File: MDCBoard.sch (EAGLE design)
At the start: 201 parts, among them J1 JUMPER-SOLDER, J10 USB-C-RECEPTACLE-KOREANHRO, J2 JUMPER-SOLDER, J3 JUMPER-SOLDER, J4 JUMPER-SOLDER, J5 JST-SM02B-SRSS-TB, J6 JUMPER-SOLDER, J7 JUMPER-SOLDER, J8 JUMPER-SOLDER, J9 MICROSD-SOCKET, Q1 PMOS-NEXPERIA-SOT1220, Q2 PMOS-NEXPERIA-SOT1220, Q3 PMOS-NEXPERIA-SOT1220, Q4 DIODESINC-DMG2305UX, Q5 DIODESINC-DMG2305UX, Q6 DIODESINC-DMG2305UX, Q7 DIODESINC-DMG2305UX, Q8 DIODESINC-DMG2305UX, SW1 TACTILE-SWITCH, U1 TI-TPS2116, U10 TI-TPS22919DCK, U11 TI-TPS22919DCK, U12 TI-TPS22919DCK, U13 TI-TPS22919DCK, U14 TI-MSP430FR2433IRGE, U15 TI-TXB0102, U16 PANASONIC-EKMB110711X, U17 LATTICE-ICE40HX4K-BG121, U18 WINBOND-W25Q40EW, U19 NEXPERIA-74LVC1G98-OR-INV-INP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, U2 DIODESINC-AP7350, U20 NEXPERIA-74LVC1G98-BUFFER, U21 ON-AR0330CS1C12SPKA0, U22 ALLIANCE-AS4C8M16MSA-6BIN, U23 NEXPERIA-74LVC1G98-INVERTER, U24 STM-STM32F730, U25 DIODESINC-DT1446-04V-7, U3 NEXPERIA-74LVC1G98-NOR, U4 MICROCHIP-MCP7383X, U5 NEXPERIA-74LVC1G98-INVERTER, U6 EATON-STN101, U7 TI-TPS62A01, U8 TI-TPS62A01, U9 TI-TPS62A01, X1 EPSON-FC-135, X2 SITIME-SIT8021, X3 SITIME-SIT8021

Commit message: Update comment
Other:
- note added: "Resistor limits drive strength to limit inrush current. If the gate resistance is too low, VDD_A will droop and MSP430 will brown out. Originally we used a 10k here, but found that the VDD_BAT drooped ~500mV when the MOSFET turned on. At 365k, VDD_BAT droops ~30mV."
- note removed: "Limits drive strength to limit inrush current. If the gate resistance is too low, VDD_A will droop and MSP430 will brown out."
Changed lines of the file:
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@@
 <wire x1="355.6" y1="444.5" x2="287.02" y2="444.5" width="0.1524" layer="95"/>
 <text x="289.814" y="389.636" size="2.54" layer="95" align="top-left">VDD_B Control</text>
-<text x="316.992" y="410.464" size="1.016" layer="95" align="top-left">Limits drive strength to limit inrush current.
-If the gate resistance is too low, VDD_A will
-droop and MSP430 will brown out.</text>
+<text x="318.008" y="414.782" size="1.016" layer="95" align="top-left">Resistor limits drive strength to limit inrush
+current. If the gate resistance is too low,
+VDD_A will droop and MSP430 will brown out.
+Originally we used a 10k here, but found that
+the VDD_BAT drooped ~500mV when the
+MOSFET turned on. At 365k, VDD_BAT
+droops ~30mV.</text>
 <text x="181.102" y="329.438" size="1.524" layer="95" align="top-left">From Linear Tech Application Note 171 </text>
 <wire x1="177.8" y1="375.92" x2="177.8" y2="335.28" width="0.1524" layer="95"/>

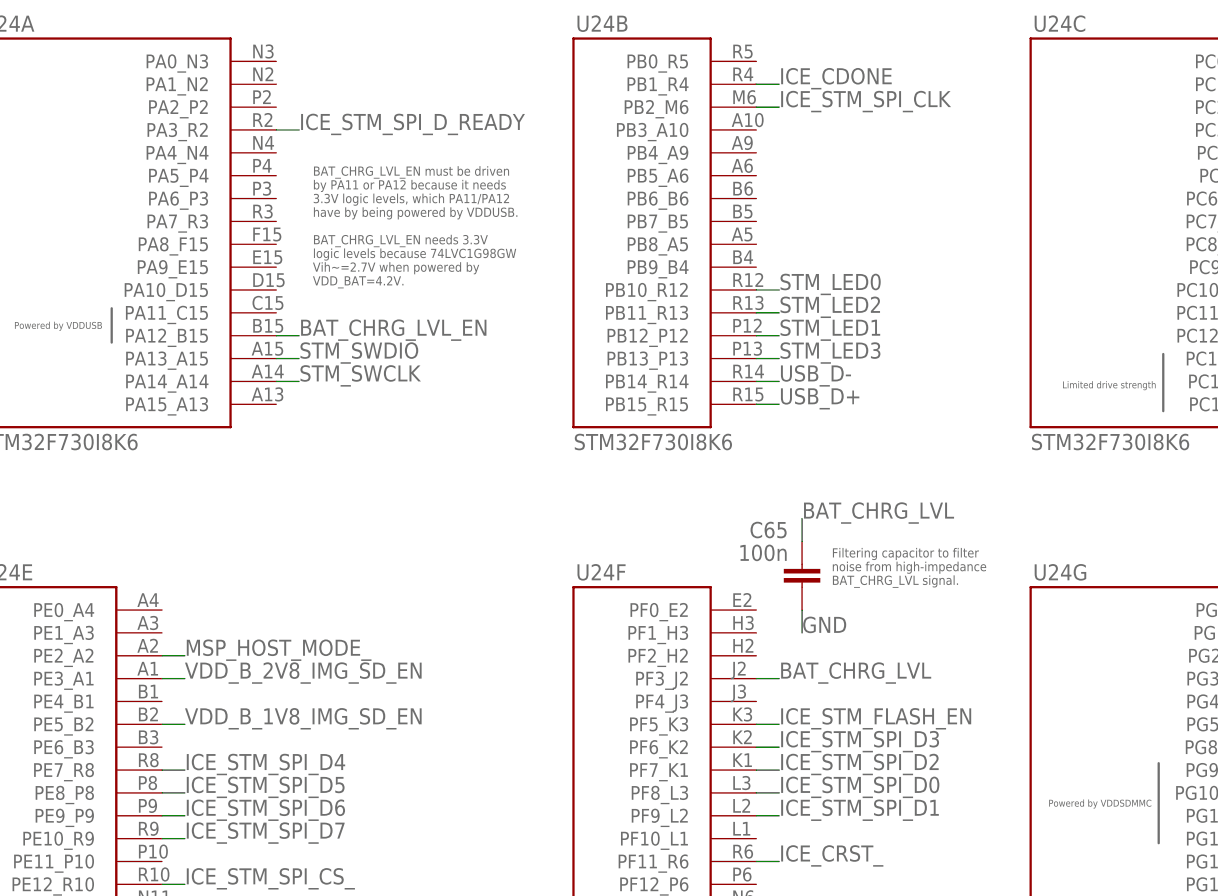
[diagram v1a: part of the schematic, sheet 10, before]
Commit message: Remove STM nets, and prepare for adding MSP<->STM comms
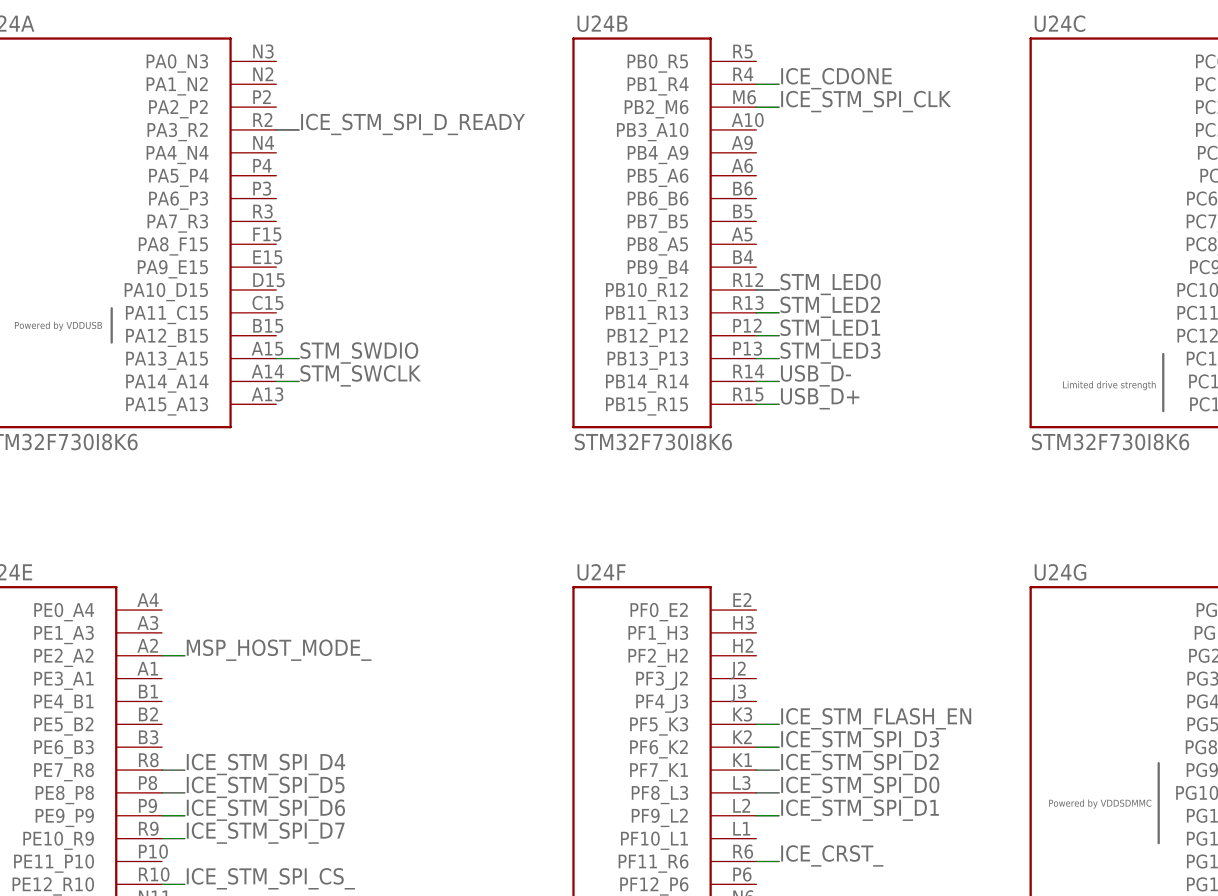
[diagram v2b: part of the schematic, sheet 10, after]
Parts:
- removed C65: 100n, EagleLibrary:CAPACITOR0402
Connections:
- net BAT_CHRG_LVL: no longer C65.1, U24F.PF3_J2
- net BAT_CHRG_LVL_EN: no longer U24A.PA12_B15
- net GND: no longer C65.2
- net VDD_B_1V8_IMG_SD_EN: no longer U24E.PE5_B2
- net VDD_B_2V8_IMG_SD_EN: no longer U24E.PE3_A1
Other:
- note removed: "BAT_CHRG_LVL_EN must be driven by PA11 or PA12 because it needs 3.3V logic levels, which PA11/PA12 have by being powered by VDDUSB. BAT_CHRG_LVL_EN needs 3.3V logic levels because 74LVC1G98GW Vih~=2.7V when powered by VDD_BAT=4.2V."
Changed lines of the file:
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@@
 <attribute name="PN" value="RT0402BRE071K8L"/>
 </part>
-<part name="C65" library="EagleLibrary" deviceset="CAPACITOR" device="0402" value="100n">
-<attribute name="MFG" value="Murata"/>
-<attribute name="PN" value="GRM155R61H104KE19D"/>
-</part>
 <part name="R6" library="EagleLibrary" deviceset="RESISTOR" device="0402" value="365k">
 <attribute name="MFG" value="Walsin"/>
@@
 <text x="67.056" y="-245.872" size="1.016" layer="95" align="top-left">Ceff&gt;1uF @ 3.3V bias</text>
 <text x="67.056" y="-220.218" size="1.016" layer="95" align="top-left">Ceff&gt;1uF @ 3.3V bias</text>
-<text x="19.304" y="-24.384" size="1.016" layer="95" align="top-left">BAT_CHRG_LVL_EN must be driven
-by PA11 or PA12 because it needs
-3.3V logic levels, which PA11/PA12
-have by being powered by VDDUSB.
-BAT_CHRG_LVL_EN needs 3.3V
-logic levels because 74LVC1G98GW
-Vih~=2.7V when powered by
-VDD_BAT=4.2V.</text>
 <text x="122.428" y="-254.762" size="0.762" layer="95" align="top-left">"If no external battery is used in the application,
 it is recommended to connect the VBAT pin to VDD"</text>
-<text x="76.962" y="-66.802" size="1.016" layer="95" align="top-left">Filtering capacitor to filter
-noise from high-impedance
-BAT_CHRG_LVL signal.</text>
 <text x="48.26" y="-258.318" size="1.778" layer="95">VDDSDMMC Bypass Capacitors</text>
 <wire x1="48.26" y1="-259.08" x2="48.26" y2="-276.86" width="0.1524" layer="95"/>
@@
 <attribute name="NAME" x="213.614" y="-80.772" size="1.778" layer="95"/>
 </instance>
-<instance part="C65" gate="G$1" x="73.66" y="-68.58" smashed="yes" rot="MR0">
-<attribute name="NAME" x="72.136" y="-65.659" size="1.778" layer="95" rot="MR0"/>
-<attribute name="VALUE" x="72.136" y="-68.199" size="1.778" layer="96" rot="MR0"/>
-</instance>
 </instances>
 <busses>
@@
 </segment>
 <segment>
-<pinref part="C65" gate="G$1" pin="2"/>
-<wire x1="73.66" y1="-73.66" x2="73.66" y2="-76.2" width="0.1524" layer="91"/>
-<label x="73.66" y="-76.2" size="1.778" layer="95"/>
-</segment>
-<segment>
 <pinref part="C86" gate="G$1" pin="2"/>
 <wire x1="66.04" y1="-271.78" x2="55.88" y2="-271.78" width="0.1524" layer="91"/>
@@
 </segment>
 </net>
-<net name="BAT_CHRG_LVL" class="0">
-<segment>
-<wire x1="68.58" y1="-81.28" x2="71.12" y2="-81.28" width="0.1524" layer="91"/>
-<label x="71.12" y="-81.28" size="1.778" layer="95"/>
-<pinref part="U24" gate="F" pin="PF3_J2"/>
-</segment>
-<segment>
-<pinref part="C65" gate="G$1" pin="1"/>
-<wire x1="73.66" y1="-66.04" x2="73.66" y2="-63.5" width="0.1524" layer="91"/>
-<label x="73.66" y="-63.5" size="1.778" layer="95"/>
-</segment>
-</net>
 <net name="ICE_STM_FLASH_EN" class="0">
 <segment>
@@
 </segment>
 </net>
-<net name="VDD_B_1V8_IMG_SD_EN" class="0">
-<segment>
-<wire x1="2.54" y1="-86.36" x2="5.08" y2="-86.36" width="0.1524" layer="91"/>
-<label x="5.08" y="-86.36" size="1.778" layer="95"/>
-<pinref part="U24" gate="E" pin="PE5_B2"/>
-</segment>
-</net>
 <net name="BAT_CHRG_STAT" class="0">
 <segment>
@@
 </segment>
 </net>
-<net name="BAT_CHRG_LVL_EN" class="0">
-<segment>
-<wire x1="15.24" y1="-43.18" x2="17.78" y2="-43.18" width="0.1524" layer="91"/>
-<label x="17.78" y="-43.18" size="1.778" layer="95"/>
-<pinref part="U24" gate="A" pin="PA12_B15"/>
-</segment>
-</net>
-<net name="VDD_B_2V8_IMG_SD_EN" class="0">
-<segment>
-<wire x1="2.54" y1="-81.28" x2="5.08" y2="-81.28" width="0.1524" layer="91"/>
-<label x="5.08" y="-81.28" size="1.778" layer="95"/>
-<pinref part="U24" gate="E" pin="PE3_A1"/>
-</segment>
-</net>

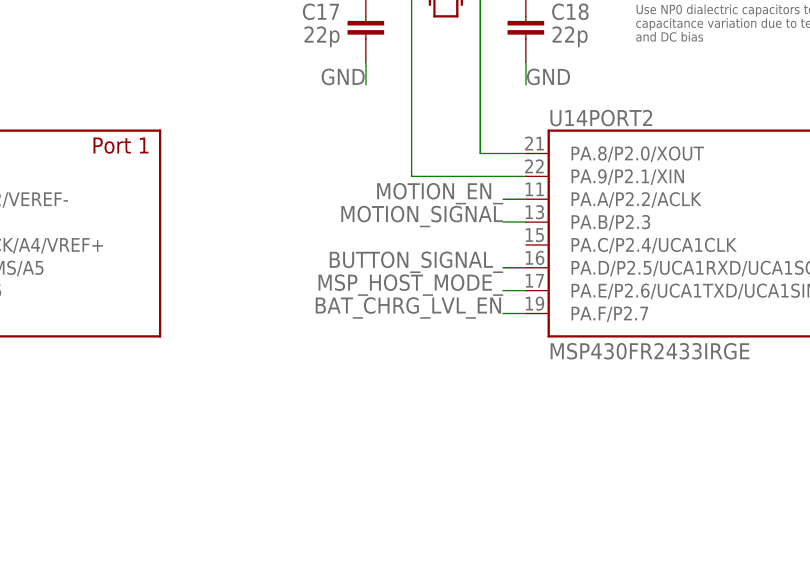
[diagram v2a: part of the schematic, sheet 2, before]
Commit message: Remove MSP_HOST_MODE_
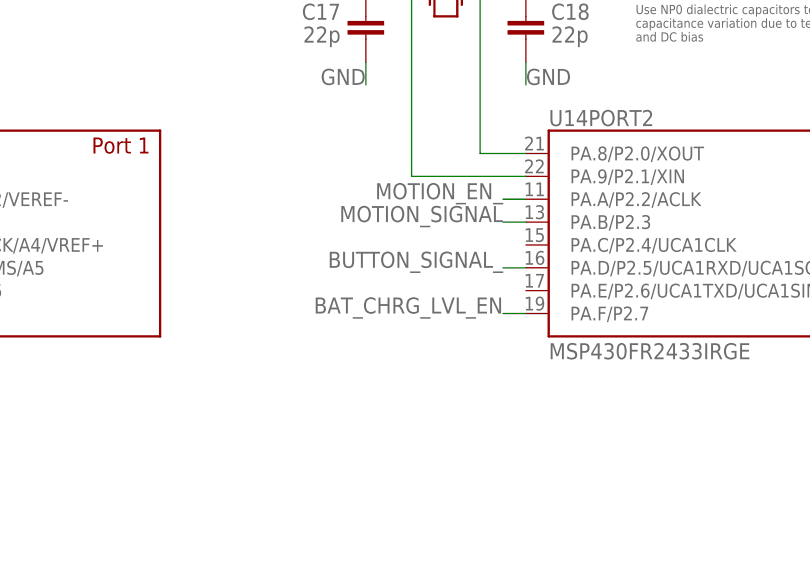
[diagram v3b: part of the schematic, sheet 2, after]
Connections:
- removed net MSP_HOST_MODE_: U14PORT2.PA.E/P2.6/UCA1TXD/UCA1SIMO, U24E.PE2_A2
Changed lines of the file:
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@@
 </segment>
 </net>
-<net name="MSP_HOST_MODE_" class="0">
-<segment>
-<wire x1="261.62" y1="68.58" x2="259.08" y2="68.58" width="0.1524" layer="91"/>
-<label x="259.08" y="68.58" size="1.778" layer="95" align="bottom-right"/>
-<pinref part="U14" gate="PORT2" pin="PA.E/P2.6/UCA1TXD/UCA1SIMO"/>
-</segment>
-</net>
 <net name="ICE_MSP_SPI_CLK" class="0">
 <segment>
@@
 </segment>
 </net>
-<net name="MSP_HOST_MODE_" class="0">
-<segment>
-<wire x1="2.54" y1="-78.74" x2="5.08" y2="-78.74" width="0.1524" layer="91"/>
-<label x="5.08" y="-78.74" size="1.778" layer="95"/>
-<pinref part="U24" gate="E" pin="PE2_A2"/>
-</segment>
-</net>

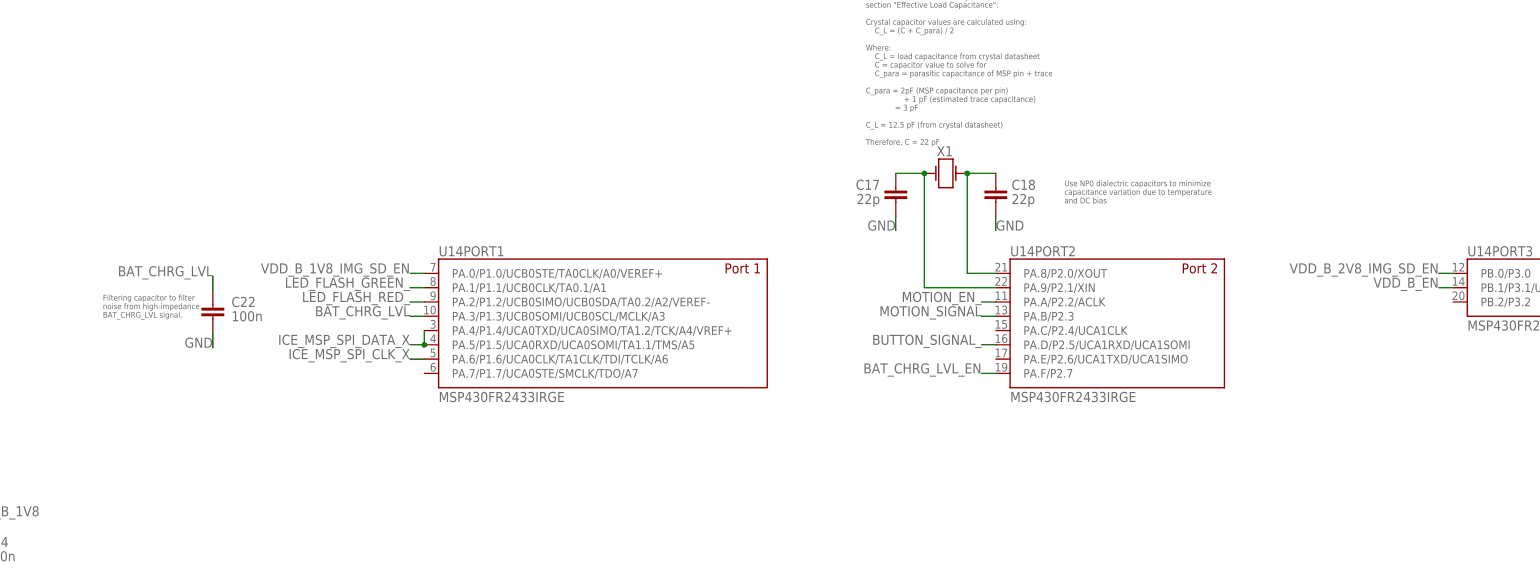
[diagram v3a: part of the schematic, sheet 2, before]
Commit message: Wired up MSP<->STM I2C comms, and added pullup resistors
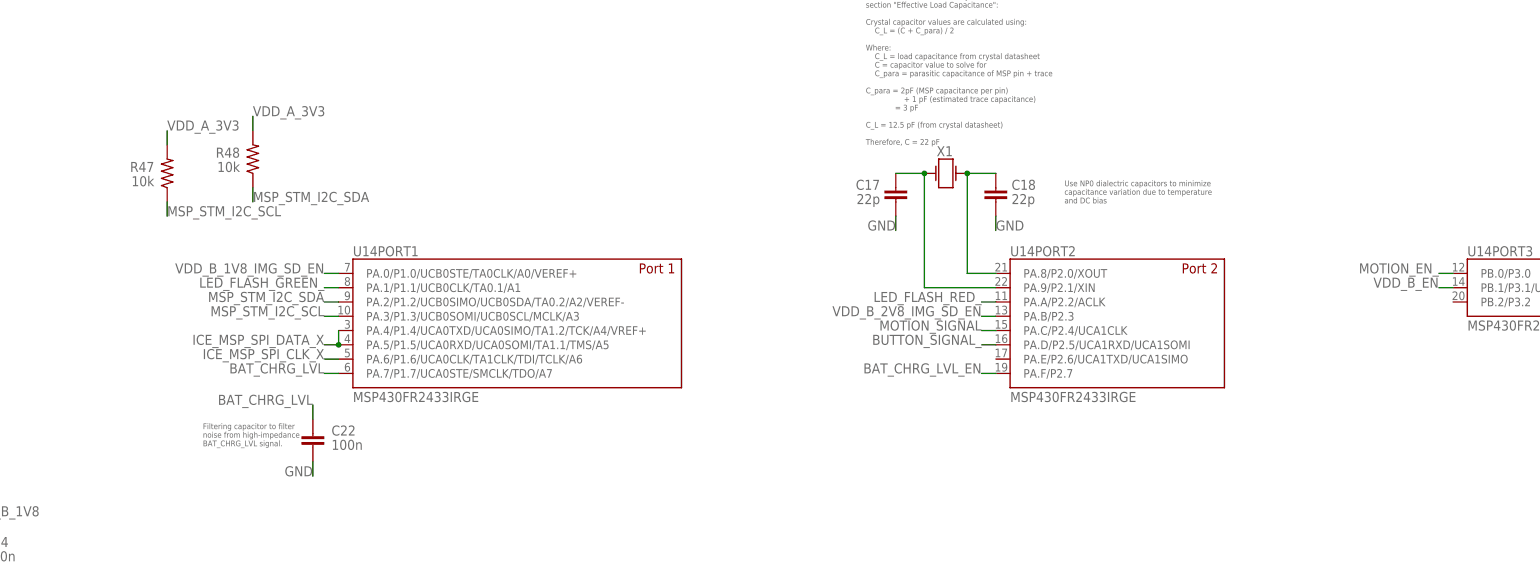
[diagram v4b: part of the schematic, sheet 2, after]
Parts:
- added R47, R48: 10k, EagleLibrary:RESISTOR0402
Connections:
- new net MSP_STM_I2C_SCL: R47.1, U14PORT1.PA.3/P1.3/UCB0SOMI/UCB0SCL/MCLK/A3, U24B.PB8_A5
- new net MSP_STM_I2C_SDA: R48.1, U14PORT1.PA.2/P1.2/UCB0SIMO/UCB0SDA/TA0.2/A2/VEREF-, U24B.PB9_B4
- net BAT_CHRG_LVL: now also U14PORT1.PA.7/P1.7/UCA0STE/SMCLK/TDO/A7; no longer U14PORT1.PA.3/P1.3/UCB0SOMI/UCB0SCL/MCLK/A3
- net LED_FLASH_RED_: now also U14PORT2.PA.A/P2.2/ACLK; no longer U14PORT1.PA.2/P1.2/UCB0SIMO/UCB0SDA/TA0.2/A2/VEREF-
- net MOTION_EN_: now also U14PORT3.PB.0/P3.0; no longer U14PORT2.PA.A/P2.2/ACLK
- net MOTION_SIGNAL: now also U14PORT2.PA.C/P2.4/UCA1CLK; no longer U14PORT2.PA.B/P2.3
- net VDD_A_3V3: now also R47.2, R48.2
- net VDD_B_2V8_IMG_SD_EN: now also U14PORT2.PA.B/P2.3; no longer U14PORT3.PB.0/P3.0
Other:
- moved on the sheet: C22, U14PORT1

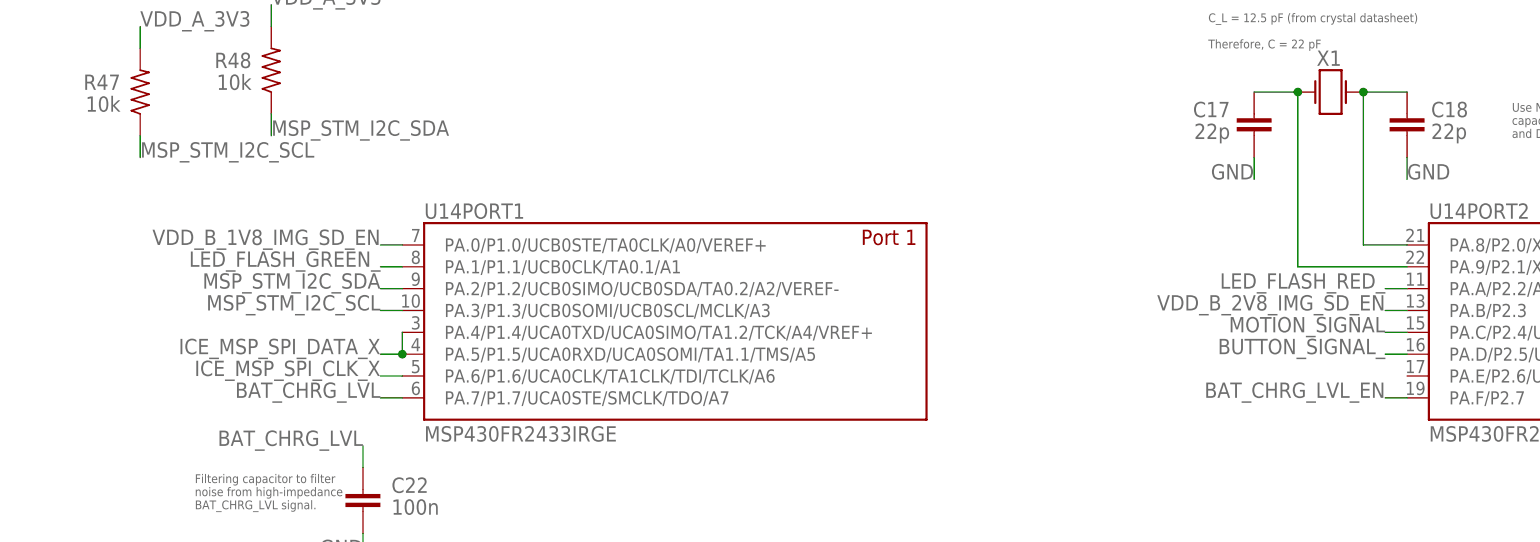
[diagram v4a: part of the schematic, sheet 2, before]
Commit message: Rename LED_FLASH_X_ -> LED_X_
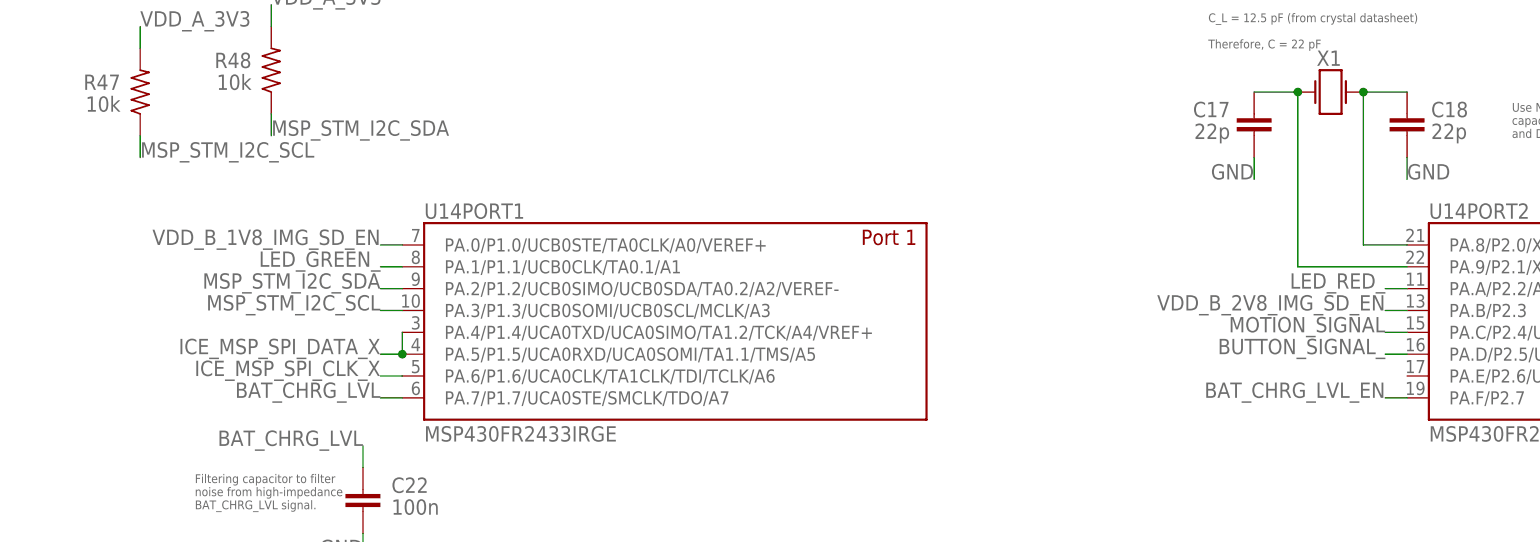
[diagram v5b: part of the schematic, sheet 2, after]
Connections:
- net LED_FLASH_GREEN_ renamed LED_GREEN_
- net LED_FLASH_RED_ renamed LED_RED_
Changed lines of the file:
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@@
 </segment>
 </net>
-<net name="LED_FLASH_GREEN_" class="0">
+<net name="LED_GREEN_" class="0">
 <segment>
 <wire x1="144.78" y1="81.28" x2="142.24" y2="81.28" width="0.1524" layer="91"/>
@@
 </segment>
 </net>
-<net name="LED_FLASH_RED_" class="0">
+<net name="LED_RED_" class="0">
 <segment>
 <wire x1="261.62" y1="78.74" x2="259.08" y2="78.74" width="0.1524" layer="91"/>
@@
 </segment>
 </net>
-<net name="LED_FLASH_RED_" class="0">
+<net name="LED_RED_" class="0">
 <segment>
 <pinref part="Q5" gate="G$1" pin="G"/>
@@
 </segment>
 </net>
-<net name="LED_FLASH_GREEN_" class="0">
+<net name="LED_GREEN_" class="0">
 <segment>
 <pinref part="Q4" gate="G$1" pin="G"/>
